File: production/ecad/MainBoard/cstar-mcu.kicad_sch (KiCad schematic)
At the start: 74 parts, among them J1 USB_C_Receptacle_USB2.0, J2 USB_C_Receptacle_USB2.0, J3 RX connect, J4 TX connect, J5 Ultra_1, J6 Ultra_2, J7 Ultra_3, J8 Ultra_4, Q1 AO3400A, Q2 AO3400A, Q3 AO3400A, Q4 AO3400A, Q5 AO3400A, Q6 AO3400A, Q7 AO3400A, Q8 AO3400A, SW1 SW_Push, SW2 SW_Push, SW3 SW_Push, SW4 SW_Push, U1 ESP32-WROOM-32UE_M113EH6400UH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, U2 CP2102N-A01-GQFN28, U4 CP2102N-A01-GQFN28, U6 ESP32-WROOM-32UE_M113EH6400UH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

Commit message: changes
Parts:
- removed Q5, Q6, Q7, Q8: AO3400A, Package_TO_SOT_SMD:SOT-23, symbol Transistor_FET:AO3400A
- removed R14, R18, R27, R28, R29, R30, R39, R40, R41, R42: 10k, Resistor_SMD:R_0805_2012Metric, symbol Device:R
- removed R31, R33, R37: 1.7k, Resistor_SMD:R_0805_2012Metric, symbol Device:R
- removed R32, R34, R38: 3.3k, Resistor_SMD:R_0805_2012Metric, symbol Device:R
- added C10, C12: 0.1uF, symbol Device:C
- added C11, C9: 10uF, symbol Device:C
- added U3, U5: TXB0104DR, D14, symbol TXB0104DR:TXB0104DR
- C1, C2, C3, C4, C5, C6, C7, C8: footprint Capacitor_SMD:C_0805_2012Metric -> (none)
- J1, J2, J3, J4, J5, J6, J7, J8: footprint Inductor_SMD:L_0805_2012Metric -> (none)
- R1, R10, R11, R12, R13, R15, R16, R17, R19, R2, R20, R21, R22, R23, R24, R25, R26, R3, R35, R36, R4, R5, R6, R7, R8, R9: footprint Resistor_SMD:R_0805_2012Metric -> (none)
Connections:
- net +3V3: now also C10.1, C11.1, C12.1, C9.1; no longer U1.2 (3V3), U6.2 (3V3)
- net +5V: now also U3.14 (VCCB), U5.14 (VCCB)
- net GND: now also U3.7 (GND), U5.7 (GND)
- net echo_1: now also U5.13 (B1); no longer U6.9 (IO33)
- net echo_2: now also U5.12 (B2); no longer U6.12 (IO27)
- net echo_3: now also U5.11 (B3); no longer U6.10 (IO25)
- net echo_4: now also U5.10 (B4); no longer U6.36 (IO22)
- net nSLEEP: now also U6.8 (IO32); no longer U1.30 (IO18)
- net trig_1: now also U3.2 (A1)
- net trig_2: now also U3.3 (A2)
- net trig_3: now also U3.4 (A3)
- net trig_4: now also U3.5 (A4)
- net 5V Trig 1 renamed 5V_trig_1
- net 5V_trig_1: now also U3.13 (B1)
- net 5V Trig 2 renamed 5V_trig_2
- net 5V_trig_2: now also U3.12 (B2)
- net 5V Trig 3 renamed 5V_trig_3
- net 5V_trig_3: now also U3.11 (B3)
- net 5V Trig 4 renamed 5V_trig_4
- net 5V_trig_4: now also U3.10 (B4)
- net USB+ renamed USB1_D+
- net USB- renamed USB1_D-
- net USB2+ renamed USB2_D+
- net USB2- renamed USB2_D-
- net VBUS renamed VBUS_1
- new net: C11.2, C12.2, U6.2 (3V3)
- new net: C10.2, C9.2, U1.2 (3V3)
- new net +3.3V: U3.1 (VCCA), U5.1 (VCCA)
- new net 3V_echo_1: U5.2 (A1), U6.9 (IO33)
- new net 3V_echo_2: U5.3 (A2), U6.12 (IO27)
- new net 3V_echo_3: U5.4 (A3), U6.10 (IO25)
- new net 3V_echo_4: U5.5 (A4), U6.36 (IO22)
- no-connect marks 36 -> 56
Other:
- moved on the sheet: J3, J4, J5, J6, J7, J8

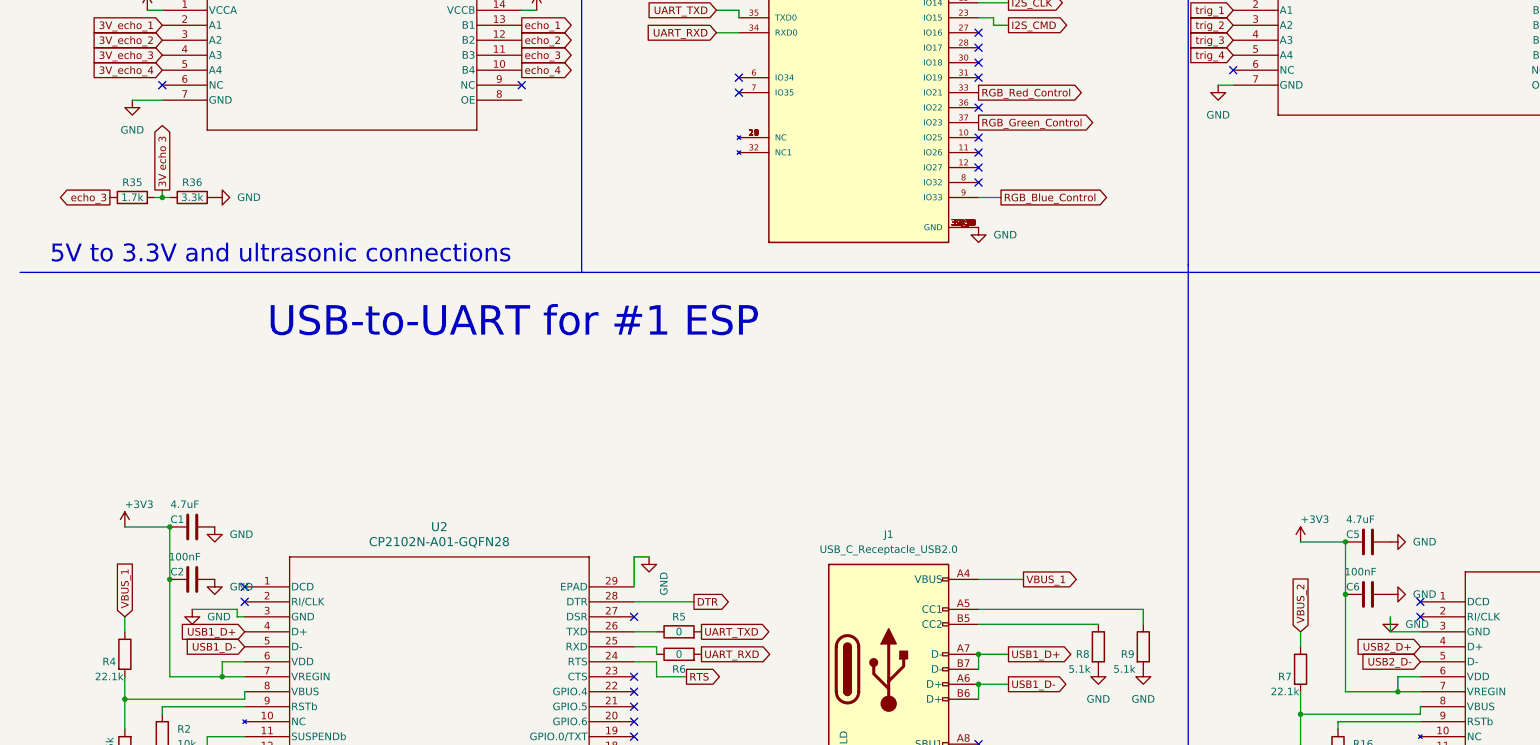
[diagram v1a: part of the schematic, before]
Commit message: footprints for resistors and capacitors
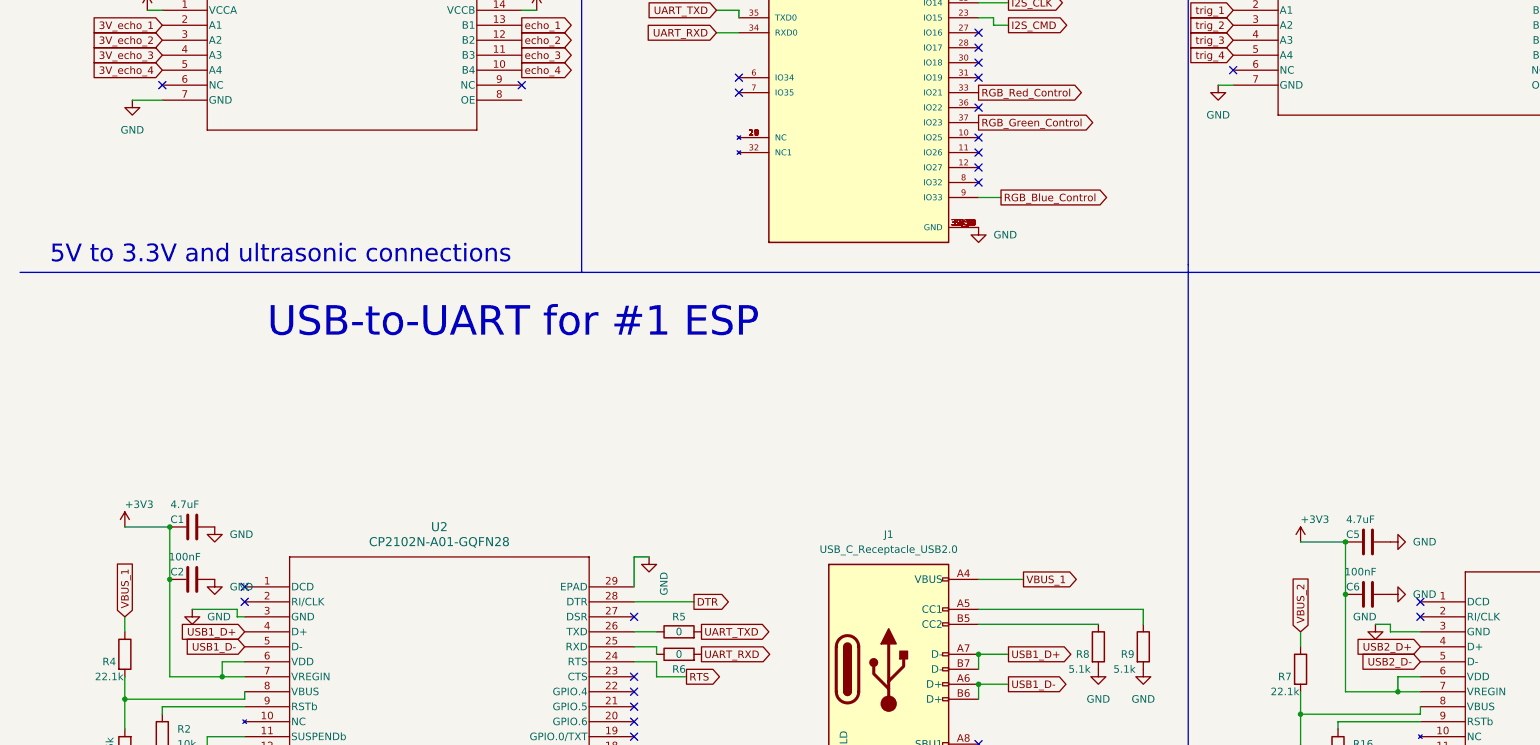
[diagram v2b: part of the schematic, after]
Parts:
- removed R35: 1.7k, symbol Device:R
- removed R36: 3.3k, symbol Device:R
- C1, C10, C11, C12, C2, C3, C4, C5, C6, C7, C8, C9: footprint (none) -> Capacitor_SMD:C_0805_2012Metric
- R1, R10, R11, R12, R13, R15, R16, R17, R19, R2, R20, R21, R22, R23, R24, R25, R26, R3, R4, R5, R6, R7, R8, R9: footprint (none) -> Resistor_SMD:R_0805_2012Metric

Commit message: finished assigning footprints
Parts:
- J1, J2: footprint (none) -> USB4105GFA:GCT_USB4105GFA
- J3, J4: footprint (none) -> Connector_PinHeader_2.54mm:PinHeader_1x02_P2.54mm_Vertical
- J5, J6, J7, J8: footprint (none) -> Connector_PinHeader_2.54mm:PinHeader_1x04_P2.54mm_Vertical
- SW1, SW2, SW3, SW4: footprint (none) -> switch:SW_1825910-6-4

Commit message: pin connector footprints
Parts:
- J3, J4: footprint Connector_PinHeader_2.54mm:PinHeader_1x02_P2.54mm_Vertical -> 2pins:CONN2_440054-2_TYC
- J5, J6, J7, J8: footprint Connector_PinHeader_2.54mm:PinHeader_1x04_P2.54mm_Vertical -> 4pinconnectors_footprint:CONN_B4B-XH-A_JST
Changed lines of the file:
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@@
       (effects (font (size 1.27 1.27)) (justify left))
     )
-    (property "Footprint" "Connector_PinHeader_2.54mm:PinHeader_1x04_P2.54mm_Vertical" (at 87.63 17.78 0)
+    (property "Footprint" "4pinconnectors_footprint:CONN_B4B-XH-A_JST" (at 87.63 17.78 0)
       (effects (font (size 1.27 1.27)) hide)
     )
@@
       (effects (font (size 1.27 1.27)) (justify left))
     )
-    (property "Footprint" "Connector_PinHeader_2.54mm:PinHeader_1x04_P2.54mm_Vertical" (at 58.42 17.78 0)
+    (property "Footprint" "4pinconnectors_footprint:CONN_B4B-XH-A_JST" (at 58.42 17.78 0)
       (effects (font (size 1.27 1.27)) hide)
     )
@@
       (effects (font (size 1.27 1.27)) (justify left))
     )
-    (property "Footprint" "Connector_PinHeader_2.54mm:PinHeader_1x02_P2.54mm_Vertical" (at 92.71 29.21 0)
+    (property "Footprint" "2pins:CONN2_440054-2_TYC" (at 92.71 29.21 0)
       (effects (font (size 1.27 1.27)) hide)
     )
@@
       (effects (font (size 1.27 1.27)) (justify left))
     )
-    (property "Footprint" "Connector_PinHeader_2.54mm:PinHeader_1x04_P2.54mm_Vertical" (at 29.21 17.78 0)
+    (property "Footprint" "4pinconnectors_footprint:CONN_B4B-XH-A_JST" (at 29.21 17.78 0)
       (effects (font (size 1.27 1.27)) hide)
     )
@@
       (effects (font (size 1.27 1.27)) (justify left))
     )
-    (property "Footprint" "Connector_PinHeader_2.54mm:PinHeader_1x04_P2.54mm_Vertical" (at 29.21 31.75 0)
+    (property "Footprint" "4pinconnectors_footprint:CONN_B4B-XH-A_JST" (at 29.21 31.75 0)
       (effects (font (size 1.27 1.27)) hide)
     )
@@
       (effects (font (size 1.27 1.27)) (justify left))
     )
-    (property "Footprint" "Connector_PinHeader_2.54mm:PinHeader_1x02_P2.54mm_Vertical" (at 62.23 27.94 0)
-      (effects (font (size 1.27 1.27)) hide)
-    )
+    (property "Footprint" "2pins:CONN2_440054-2_TYC" (at 62.23 27.94 0)
+      (effects (font (size 1.27 1.27)) hide)
+    )

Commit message: footprint assignments
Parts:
- J1, J2: footprint USB4105GFA:GCT_USB4105GFA -> CSTAR-MainBoard-Footprints:USBCONN-GCT_USB4105GFA
- J3, J4: footprint 2pins:CONN2_440054-2_TYC -> Connector_PinHeader_2.54mm:PinHeader_1x02_P2.54mm_Vertical
- J5, J6, J7, J8: footprint 4pinconnectors_footprint:CONN_B4B-XH-A_JST -> CSTAR-MainBoard-Footprints:B4B_PH_K_S
- SW1, SW2, SW3, SW4: footprint switch:SW_1825910-6-4 -> CSTAR-MainBoard-Footprints:SW_1825910-6-4
- U1, U6: footprint ESP32-WROOM-32UE_M113EH6400UH3Q0_:MODULE_ESP32-WROOM-32UE_M113EH6400UH3Q0_ -> CSTAR-MainBoard-Footprints:MODULE_ESP32-WROOM-32UE_M113EH6400UH3Q0_
- U2: footprint QFN28_5X5_SIL -> CSTAR-MainBoard-Footprints:SW_1825910-6-4
- U3, U5: footprint D14 -> CSTAR-MainBoard-Footprints:D14
- U4: footprint QFN28_5X5_SIL -> CSTAR-MainBoard-Footprints:691137710002-2CONN

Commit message: footprint assign more
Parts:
- U2: footprint CSTAR-MainBoard-Footprints:SW_1825910-6-4 -> CSTAR-MainBoard-Footprints:QFN28_5X5_SIL
- U4: footprint CSTAR-MainBoard-Footprints:691137710002-2CONN -> CSTAR-MainBoard-Footprints:QFN28_5X5_SIL
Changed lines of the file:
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@@
       (effects (font (size 1.524 1.524)))
     )
-    (property "Footprint" "CSTAR-MainBoard-Footprints:SW_1825910-6-4" (at 49.53 149.86 0)
+    (property "Footprint" "CSTAR-MainBoard-Footprints:QFN28_5X5_SIL" (at 49.53 149.86 0)
       (effects (font (size 1.27 1.27) italic) hide)
     )
@@
       (effects (font (size 1.524 1.524)))
     )
-    (property "Footprint" "CSTAR-MainBoard-Footprints:691137710002-2CONN" (at 248.92 152.4 0)
+    (property "Footprint" "CSTAR-MainBoard-Footprints:QFN28_5X5_SIL" (at 248.92 152.4 0)
       (effects (font (size 1.27 1.27) italic) hide)
     )
